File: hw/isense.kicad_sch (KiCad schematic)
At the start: 4 parts, among them U3 INA240A2D

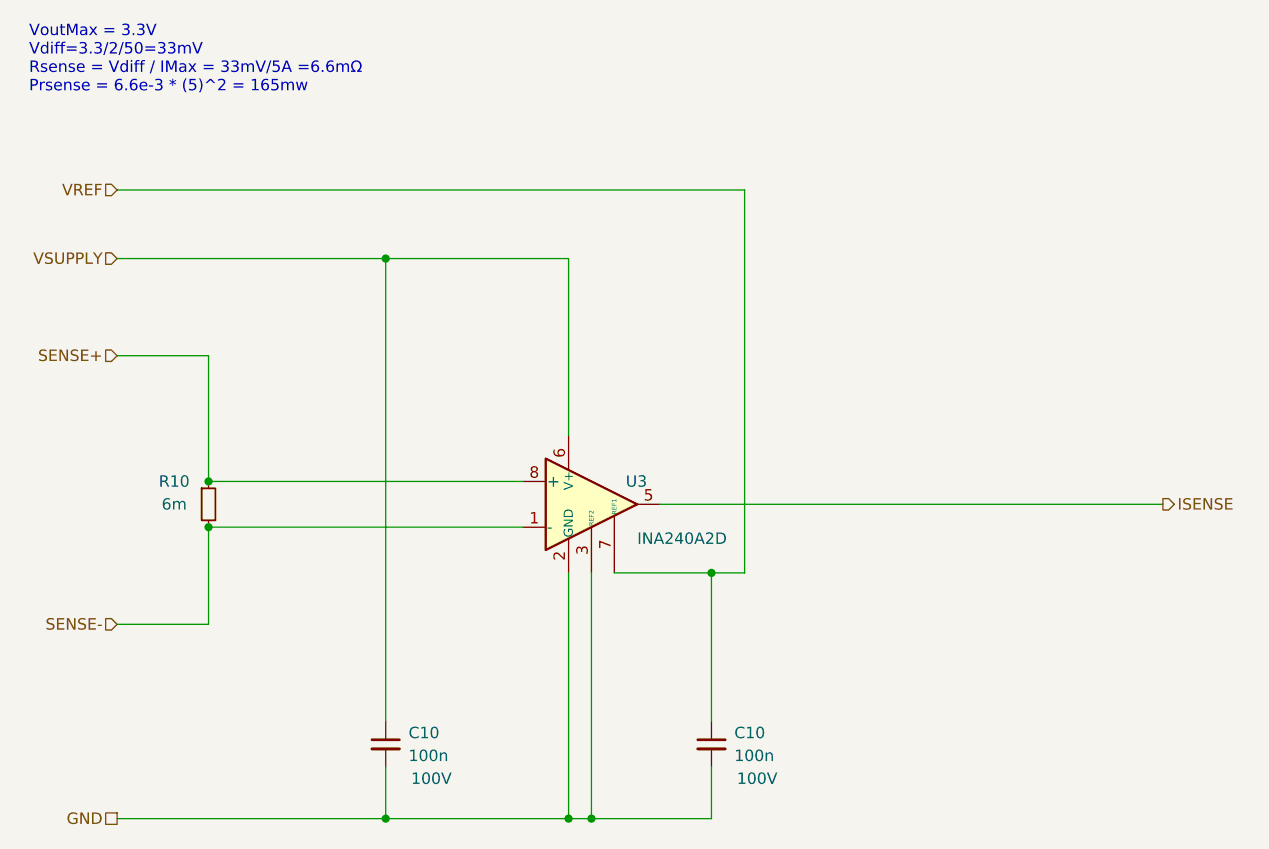
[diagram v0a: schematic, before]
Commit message: [Hw] No iso can, 0402 where possible, approx layout and formfactor
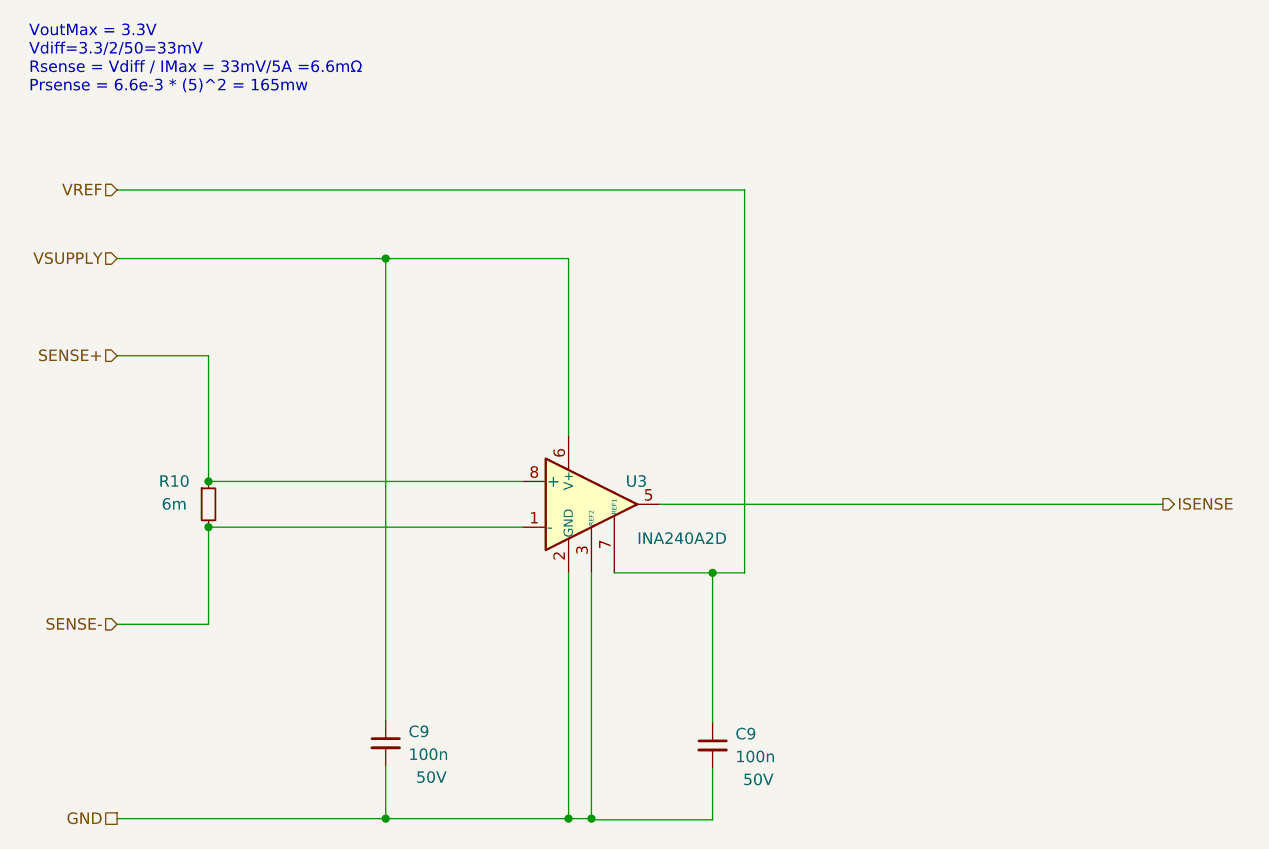
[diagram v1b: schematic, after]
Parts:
- removed C10 (x2): 100n, Capacitor_SMD:C_0603_1608Metric, symbol Device:C_Small
- added C9 (x2): 100n, Capacitor_SMD:C_0402_1005Metric, symbol Device:C_Small
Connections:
- net GND: now also C9.2, C9.2
- net VREF: now also C9.1
- net VSUPPLY: now also C9.1
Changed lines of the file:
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@@
   (junction (at 95.885 108.585) (diameter 0) (color 0 0 0 0)
   )
+  (junction (at 151.892 113.665) (diameter 0) (color 0 0 0 0)
+  )
+  (junction (at 135.89 140.97) (diameter 0) (color 0 0 0 0)
+  )
+  (junction (at 115.57 140.97) (diameter 0) (color 0 0 0 0)
+  )
+  (junction (at 95.885 103.505) (diameter 0) (color 0 0 0 0)
+  )
   (junction (at 115.57 78.74) (diameter 0) (color 0 0 0 0)
   )
-  (junction (at 135.89 140.97) (diameter 0) (color 0 0 0 0)
-  )
-  (junction (at 115.57 140.97) (diameter 0) (color 0 0 0 0)
-  )
-  (junction (at 151.765 113.665) (diameter 0) (color 0 0 0 0)
-  )
-  (junction (at 95.885 103.505) (diameter 0) (color 0 0 0 0)
-  )
   (wire (pts (xy 201.93 106.045) (xy 146.05 106.045))
     (stroke (width 0) (type default))
   )
-  (wire (pts (xy 151.765 135.255) (xy 151.765 140.97))
-    (stroke (width 0) (type default))
-  )
-  (wire (pts (xy 151.765 113.665) (xy 151.765 130.175))
+  (wire (pts (xy 151.892 135.382) (xy 151.892 141.097))
+    (stroke (width 0) (type default))
+  )
+  (wire (pts (xy 138.43 141.097) (xy 138.43 140.97))
+    (stroke (width 0) (type default))
+  )
+  (wire (pts (xy 151.892 113.665) (xy 151.892 130.302))
     (stroke (width 0) (type default))
   )
@@
     (stroke (width 0) (type default))
   )
-  (wire (pts (xy 151.765 113.665) (xy 140.97 113.665))
+  (wire (pts (xy 115.57 78.74) (xy 135.89 78.74))
     (stroke (width 0) (type default))
   )
@@
     (stroke (width 0) (type default))
   )
-  (wire (pts (xy 115.57 78.74) (xy 135.89 78.74))
+  (wire (pts (xy 85.725 78.74) (xy 115.57 78.74))
     (stroke (width 0) (type default))
   )
@@
     (stroke (width 0) (type default))
   )
-  (wire (pts (xy 115.57 135.255) (xy 115.57 140.97))
-    (stroke (width 0) (type default))
-  )
-  (wire (pts (xy 155.448 113.665) (xy 151.765 113.665))
+  (wire (pts (xy 115.57 135.128) (xy 115.57 140.97))
+    (stroke (width 0) (type default))
+  )
+  (wire (pts (xy 155.448 113.665) (xy 151.892 113.665))
     (stroke (width 0) (type default))
   )
@@
     (stroke (width 0) (type default))
   )
-  (wire (pts (xy 85.725 78.74) (xy 115.57 78.74))
-    (stroke (width 0) (type default))
-  )
-  (wire (pts (xy 115.57 78.74) (xy 115.57 130.175))
-    (stroke (width 0) (type default))
-  )
-  (wire (pts (xy 151.765 140.97) (xy 138.43 140.97))
+  (wire (pts (xy 151.892 141.097) (xy 138.43 141.097))
+    (stroke (width 0) (type default))
+  )
+  (wire (pts (xy 140.97 113.665) (xy 151.892 113.665))
     (stroke (width 0) (type default))
   )
@@
   )
   (wire (pts (xy 155.448 71.12) (xy 155.448 113.665))
+    (stroke (width 0) (type default))
+  )
+  (wire (pts (xy 115.57 78.74) (xy 115.57 130.048))
     (stroke (width 0) (type default))
   )
@@
     (effects (font (size 1.27 1.27)) (justify right))
   )
-  (symbol (lib_id "Device:C_Small") (at 151.765 132.715 0) (unit 1)
-    (in_bom yes) (on_board yes) (dnp no)
-    (property "Reference" "C10" (at 154.305 131.445 0)
-      (effects (font (size 1.27 1.27)) (justify left))
-    )
-    (property "Value" "100n" (at 154.305 133.985 0)
-      (effects (font (size 1.27 1.27)) (justify left))
-    )
-    (property "Footprint" "Capacitor_SMD:C_0603_1608Metric" (at 151.765 132.715 0)
-      (effects (font (size 1.27 1.27)) hide)
-    )
-    (property "Datasheet" "~" (at 151.765 132.715 0)
-      (effects (font (size 1.27 1.27)) hide)
-    )
-    (property "Rating" "100V" (at 156.845 136.525 0)
-      (effects (font (size 1.27 1.27)))
-    )
-    (property "LCSC" "C15725" (at 151.765 132.715 0)
-      (effects (font (size 1.27 1.27)) hide)
-    )
-    (pin "1")
-    (pin "2")
-    (instances
-      (project "foc8313"
-        (path "/6a0f293a-1ae1-497a-a3c1-0d8f9e6f81b9"
-          (reference "C10") (unit 1)
+  (symbol (lib_id "Device:C_Small") (at 115.57 132.588 0) (unit 1)
+    (in_bom yes) (on_board yes) (dnp no)
+    (property "Reference" "C9" (at 118.11 131.318 0)
+      (effects (font (size 1.27 1.27)) (justify left))
+    )
+    (property "Value" "100n" (at 118.11 133.858 0)
+      (effects (font (size 1.27 1.27)) (justify left))
+    )
+    (property "Footprint" "Capacitor_SMD:C_0402_1005Metric" (at 115.57 132.588 0)
+      (effects (font (size 1.27 1.27)) hide)
+    )
+    (property "Datasheet" "~" (at 115.57 132.588 0)
+      (effects (font (size 1.27 1.27)) hide)
+    )
+    (property "Rating" "50V" (at 120.65 136.398 0)
+      (effects (font (size 1.27 1.27)))
+    )
+    (property "LCSC" "C307331" (at 115.57 132.588 0)
+      (effects (font (size 1.27 1.27)) hide)
+    )
+    (pin "1")
+    (pin "2")
+    (instances
+      (project "foc8313"
+        (path "/6a0f293a-1ae1-497a-a3c1-0d8f9e6f81b9"
+          (reference "C9") (unit 1)
+        )
+        (path "/6a0f293a-1ae1-497a-a3c1-0d8f9e6f81b9/4c6c6d09-876f-4eba-b2a4-6d544596feb9"
+          (reference "C20") (unit 1)
+        )
+        (path "/6a0f293a-1ae1-497a-a3c1-0d8f9e6f81b9/1cc54603-d82e-415c-bbf9-5b5f12638dae"
+          (reference "C23") (unit 1)
+        )
+        (path "/6a0f293a-1ae1-497a-a3c1-0d8f9e6f81b9/cbef46e6-2abc-49e9-9115-5032ed0b40d4"
+          (reference "C26") (unit 1)
+        )
+      )
+    )
+  )
+  (symbol (lib_id "Device:C_Small") (at 151.892 132.842 0) (unit 1)
+    (in_bom yes) (on_board yes) (dnp no)
+    (property "Reference" "C9" (at 154.432 131.572 0)
+      (effects (font (size 1.27 1.27)) (justify left))
+    )
+    (property "Value" "100n" (at 154.432 134.112 0)
+      (effects (font (size 1.27 1.27)) (justify left))
+    )
+    (property "Footprint" "Capacitor_SMD:C_0402_1005Metric" (at 151.892 132.842 0)
+      (effects (font (size 1.27 1.27)) hide)
+    )
+    (property "Datasheet" "~" (at 151.892 132.842 0)
+      (effects (font (size 1.27 1.27)) hide)
+    )
+    (property "Rating" "50V" (at 156.972 136.652 0)
+      (effects (font (size 1.27 1.27)))
+    )
+    (property "LCSC" "C307331" (at 151.892 132.842 0)
+      (effects (font (size 1.27 1.27)) hide)
+    )
+    (pin "1")
+    (pin "2")
+    (instances
+      (project "foc8313"
+        (path "/6a0f293a-1ae1-497a-a3c1-0d8f9e6f81b9"
+          (reference "C9") (unit 1)
         )
         (path "/6a0f293a-1ae1-497a-a3c1-0d8f9e6f81b9/4c6c6d09-876f-4eba-b2a4-6d544596feb9"
@@
         )
       )
-    )
-  )
-  (symbol (lib_id "Device:C_Small") (at 115.57 132.715 0) (unit 1)
-    (in_bom yes) (on_board yes) (dnp no)
-    (property "Reference" "C10" (at 118.11 131.445 0)
-      (effects (font (size 1.27 1.27)) (justify left))
-    )
-    (property "Value" "100n" (at 118.11 133.985 0)
-      (effects (font (size 1.27 1.27)) (justify left))
-    )
-    (property "Footprint" "Capacitor_SMD:C_0603_1608Metric" (at 115.57 132.715 0)
-      (effects (font (size 1.27 1.27)) hide)
-    )
-    (property "Datasheet" "~" (at 115.57 132.715 0)
-      (effects (font (size 1.27 1.27)) hide)
-    )
-    (property "Rating" "100V" (at 120.65 136.525 0)
-      (effects (font (size 1.27 1.27)))
-    )
-    (property "LCSC" "C15725" (at 115.57 132.715 0)
-      (effects (font (size 1.27 1.27)) hide)
-    )
-    (pin "1")
-    (pin "2")
-    (instances
-      (project "foc8313"
-        (path "/6a0f293a-1ae1-497a-a3c1-0d8f9e6f81b9"
-          (reference "C10") (unit 1)
-        )
-        (path "/6a0f293a-1ae1-497a-a3c1-0d8f9e6f81b9/4c6c6d09-876f-4eba-b2a4-6d544596feb9"
-          (reference "C20") (unit 1)
-        )
-        (path "/6a0f293a-1ae1-497a-a3c1-0d8f9e6f81b9/1cc54603-d82e-415c-bbf9-5b5f12638dae"
-          (reference "C23") (unit 1)
-        )
-        (path "/6a0f293a-1ae1-497a-a3c1-0d8f9e6f81b9/cbef46e6-2abc-49e9-9115-5032ed0b40d4"
-          (reference "C26") (unit 1)
-        )
-      )

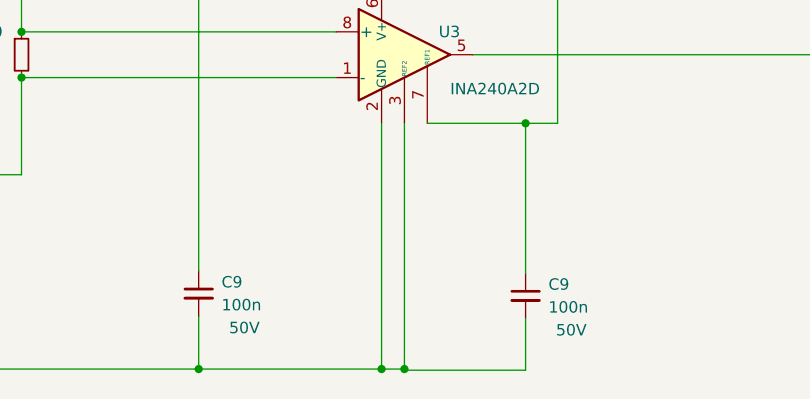
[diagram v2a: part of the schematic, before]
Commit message: [Hw] Optimised components for JLC basic parts
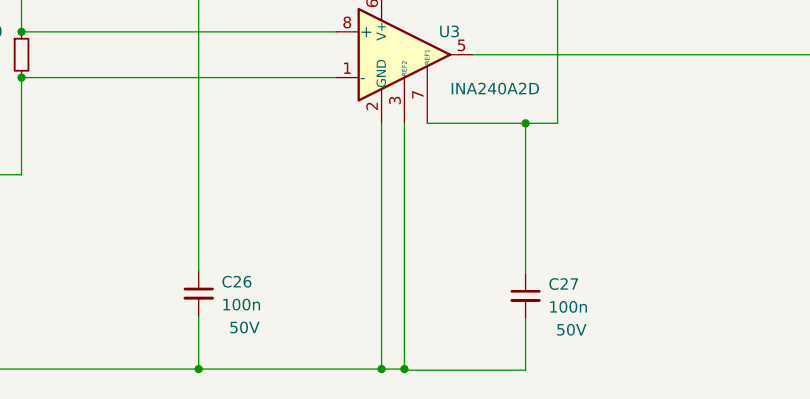
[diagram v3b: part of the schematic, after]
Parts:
- renumbered C9 to C26, C9 to C27

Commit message: [Hw] WIP begun revisions for v0.2.0
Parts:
- R10: value 6m -> 10m; LCSC C728268 -> C7467614
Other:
- note added: "VoutMax = 3.3V Vdiff=3.3/2/50=33mV Rsense = Vdiff / IMax = 33mV/2.5A =13.2mΩ Prsense = 13.2e-3 * (2.5)^2 = 82.5mw"
- note removed: "VoutMax = 3.3V Vdiff=3.3/2/50=33mV Rsense = Vdiff / IMax = 33mV/5A =6.6mΩ Prsense = 6.6e-3 * (5)^2 = 165mw"
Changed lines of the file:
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@@
 		)
 	)
-	(text "VoutMax = 3.3V\nVdiff=3.3/2/50=33mV\nRsense = Vdiff / IMax = 33mV/5A =6.6mΩ\nPrsense = 6.6e-3 * (5)^2 = 165mw"
+	(text "VoutMax = 3.3V\nVdiff=3.3/2/50=33mV\nRsense = Vdiff / IMax = 33mV/2.5A =13.2mΩ\nPrsense = 13.2e-3 * (2.5)^2 = 82.5mw"
 		(exclude_from_sim no)
 		(at 75.946 60.452 0)
@@
 			)
 		)
-		(property "Value" "6m"
+		(property "Value" "10m"
 			(at 92.075 106.045 0)
 			(effects
@@
 			)
 		)
-		(property "LCSC" "C728268"
+		(property "LCSC" "C7467614"
 			(at 95.885 106.045 0)
 			(effects

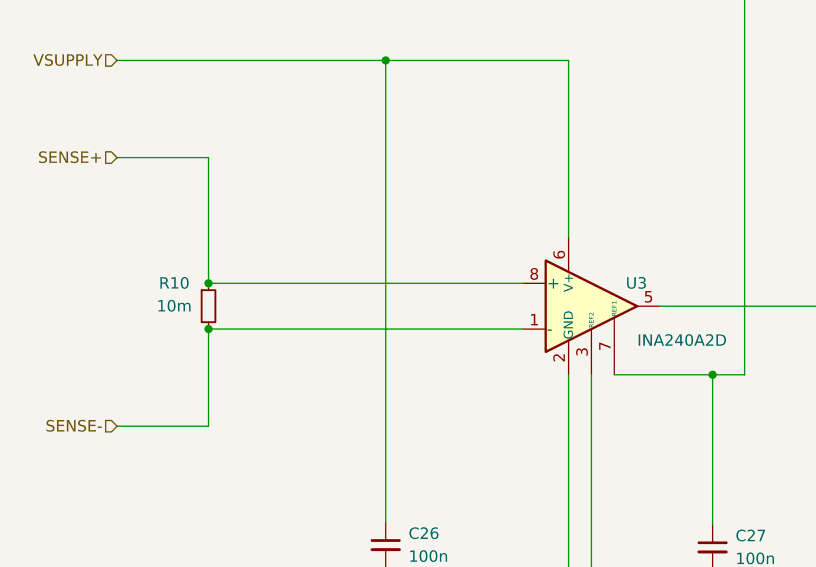
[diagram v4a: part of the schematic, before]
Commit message: [Hw] Using advanced timer for PWM generation, and general purpose for encoder input
Signed-off-by: Will Haarhoff <williamhaarhoff@gmail.com>
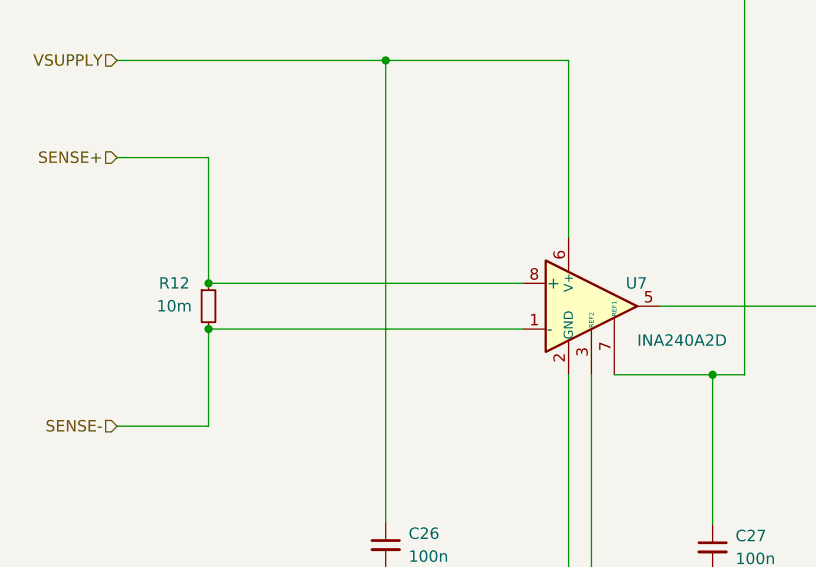
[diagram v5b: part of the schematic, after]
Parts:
- renumbered R10 to R12, U3 to U7

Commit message: [Hw] Cleaned up schematic, 10m isense shunts, green power led, DRC
Signed-off-by: Will Haarhoff <williamhaarhoff@gmail.com>
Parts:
- R12: LCSC C7467614 -> C601083
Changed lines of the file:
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@@
 			)
 		)
-		(property "LCSC" "C7467614"
+		(property "LCSC" "C601083"
 			(at 95.885 106.045 0)
 			(effects
